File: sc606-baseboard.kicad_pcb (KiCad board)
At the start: 6 copper layers, 100 x 90 mm, 454 parts, among them IC1 TPS54561DPRT, IC2 TPS7A0518PDBVT, IC3 HD3SS3220, IC4 HD3SS3220, J1 PJ-202A, J10 WE_632723300011, J11 USB-A3-C31-D-RA-CS1, J12 U_FL-R-SMT-1_10_, J13 USB-A3-C31-D-RA-CS1, J2 WE_68715014522, J3 F52R-1A7H1-11020, J4 46756-1001, J5 U_FL-R-SMT-1_10_, J6 U_FL-R-SMT-1_10_, J7 DM3AT-SF-PEJM5, J8 693022010811, J9 0473460001, M1 SC606T, Q1 BSS138APW, Q2 BSS138-7-F, Q3 BSS138APW, Q4 BSS138APW, Q5 BSS138APW, Q6 BSS138APW, Q7 BSS138-7-F, Q8 BSS138-7-F, SW1 1X03, U1 AP62301WU-7, U10 NCP163ASN330T1G, U11 EMIF06-MSD02N16, U12 FSUSB30MUX, U13 FT232RQ-REEL, U15 USB57442G, U2 AP62301WU-7, U3 AP62301WU-7, U4 74LVC1G123GN, U5 NTS0102GT, U6 PCA9547BS, U7 LT9611UXC, U8 NTS0102GT, U9 TPD13S523PWR, Y1 ABM8G-24.000MHZ-18-D2Y-T, Y2 ABM8G-25.000MHZ-B4Y-T

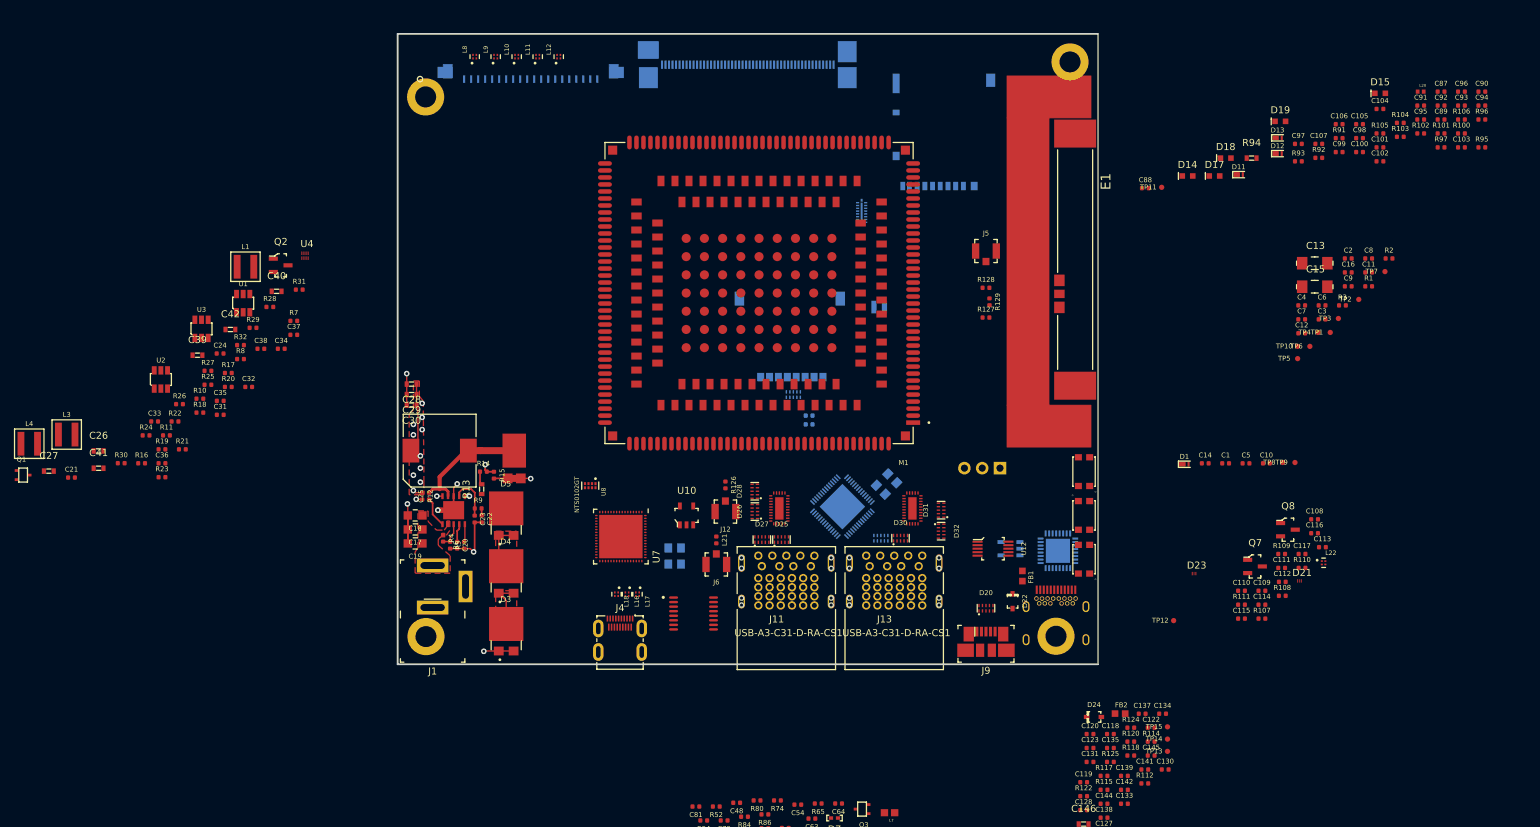
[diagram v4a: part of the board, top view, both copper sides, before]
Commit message: Added buck converters for 3v3 sys, 3v3 cam, 1v2 lontium. Added auto power-on
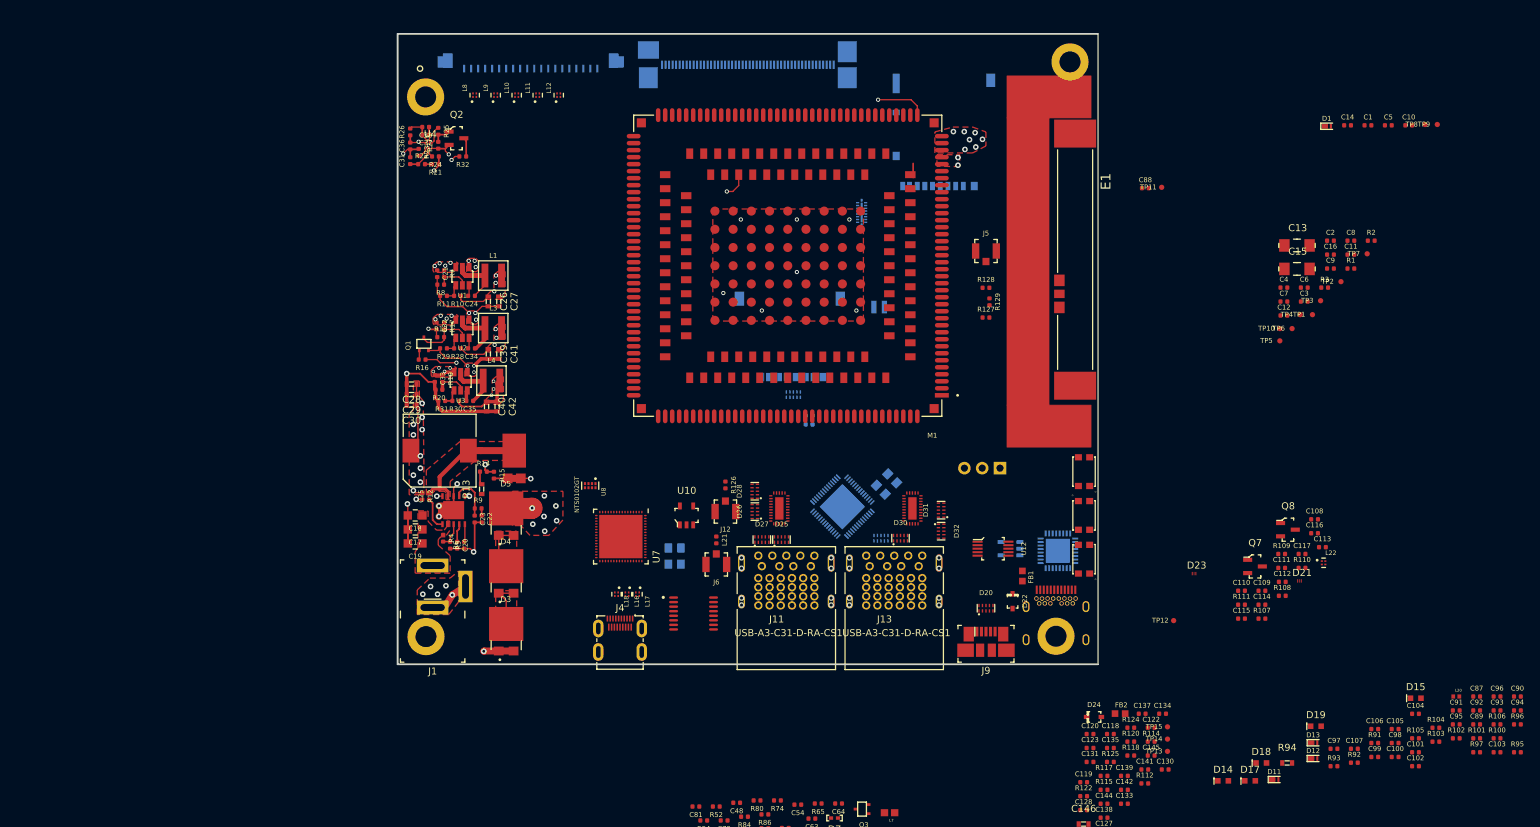
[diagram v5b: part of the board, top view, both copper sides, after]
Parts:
- C146, C158: footprint antmicro-footprints:0603-cap -> sc606-baseboard-footprints:0603-cap
- IC3, IC4: footprint antmicro-footprints:RNH0030A -> sc606-baseboard-footprints:RNH0030A
- J11, J13: footprint antmicro-footprints:USB-A3-C31-D-RA-CS1 -> sc606-baseboard-footprints:USB-A3-C31-D-RA-CS1
- R130, R131, R132, R133, R134, R135, R136, R137, R138, R139, R140, R141, R142, R143, R144, R145, R146, R147, R148, R149, R150, R151, R152, R153, R154, R159, R160, R161: footprint antmicro-footprints:0402-res -> sc606-baseboard-footprints:0402-res
- moved C100 86.5 mm to (217.4, 143.2)
- moved C102 86.5 mm to (220.3, 144.6)
- moved C89 86.5 mm to (229.1, 138.6)
- moved C95 86.5 mm to (226.1, 138.6)
- moved C99 86.5 mm to (214.5, 143.2)
- moved D11 86.5 mm to (200.2, 146.5)
- moved D12 86.5 mm to (205.7, 143.5)
- moved D13 86.5 mm to (205.7, 141.2)
- moved D14 86.5 mm to (192.9, 146.6)
- moved D17 86.5 mm to (196.7, 146.6)
- moved R103 86.5 mm to (223.2, 141.1)
- moved R106 86.5 mm to (232.0, 138.6)
- moved R92 86.5 mm to (211.6, 144.1)
- moved R93 86.5 mm to (208.7, 144.6)
- moved R96 86.5 mm to (234.9, 138.6)
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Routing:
- net V_SOM: track 0.00 -> 81.7 mm, vias 0 -> 14
- net PWRKEY: track 0.00 -> 73.1 mm, vias 0 -> 2
- net GND: track 36.2 -> 94.8 mm, vias 6 -> 33
- net CAM_RST: track 0.00 -> 56.9 mm, vias 0 -> 2
- net 3V3_SYS: track 0.00 -> 9.42 mm, vias 0 -> 3
- net 5V0_SYS: track 15.2 -> 23.8 mm, vias 11 -> 25
- net Net-(Q1-Pad3): track 0.00 -> 8.51 mm
- net Net-(C35-Pad1): track 0.00 -> 7.82 mm
- net Net-(C34-Pad1): track 0.00 -> 7.77 mm
- net Net-(C24-Pad1): track 0.00 -> 7.64 mm
- net 1V2_SYS: track 0.00 -> 4.88 mm, vias 0 -> 3
- net 3V3_CAM: track 0.00 -> 4.64 mm, vias 0 -> 3
- net Net-(R7-Pad2): track 0.00 -> 4.61 mm
- net Net-(R19-Pad2): track 0.00 -> 4.55 mm
- net Net-(C37-Pad2): track 0.00 -> 4.46 mm
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- added copper zone on F.Cu, net 1V2_SYS
- added copper zone on F.Cu, net 3V3_CAM
- added copper zone on F.Cu, net 3V3_SYS
- added copper zone on F.Cu, net GND
- added copper zone on F.Cu, net Net-(C25-Pad2)
- added copper zone on F.Cu, net V_SOM
- added copper zone on In3.5V0, net V_SOM
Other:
- net class Default: clearance 0.2 -> 0.15; trace_width 0.25 -> 0.15; via_dia 0.8 -> 0.6; via_drill 0.4 -> 0.35
- rule trace_clearance: 0.2 -> 0.15
- rule trace_min: 0.2 -> 0.15
- rule via_min_drill: 0.3 -> 0.35
- rule via_min_size: 0.4 -> 0.6

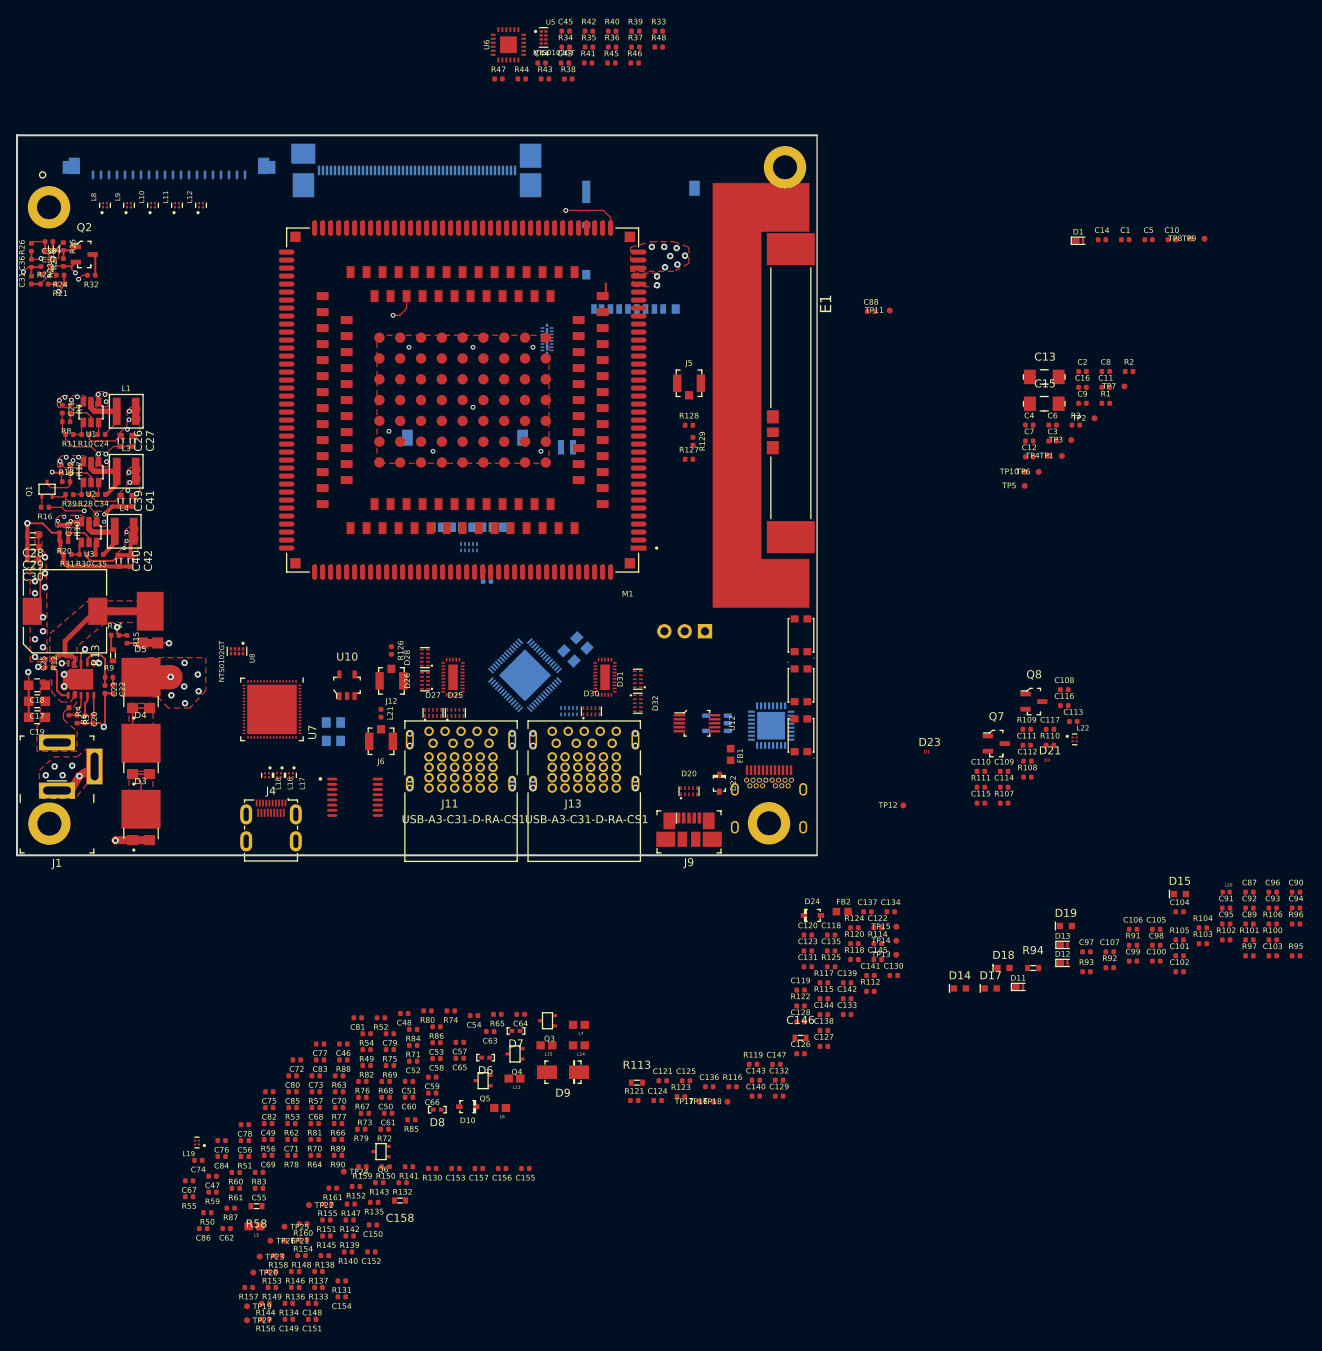
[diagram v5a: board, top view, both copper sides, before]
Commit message: FFC and general display camera connectors distributed on board
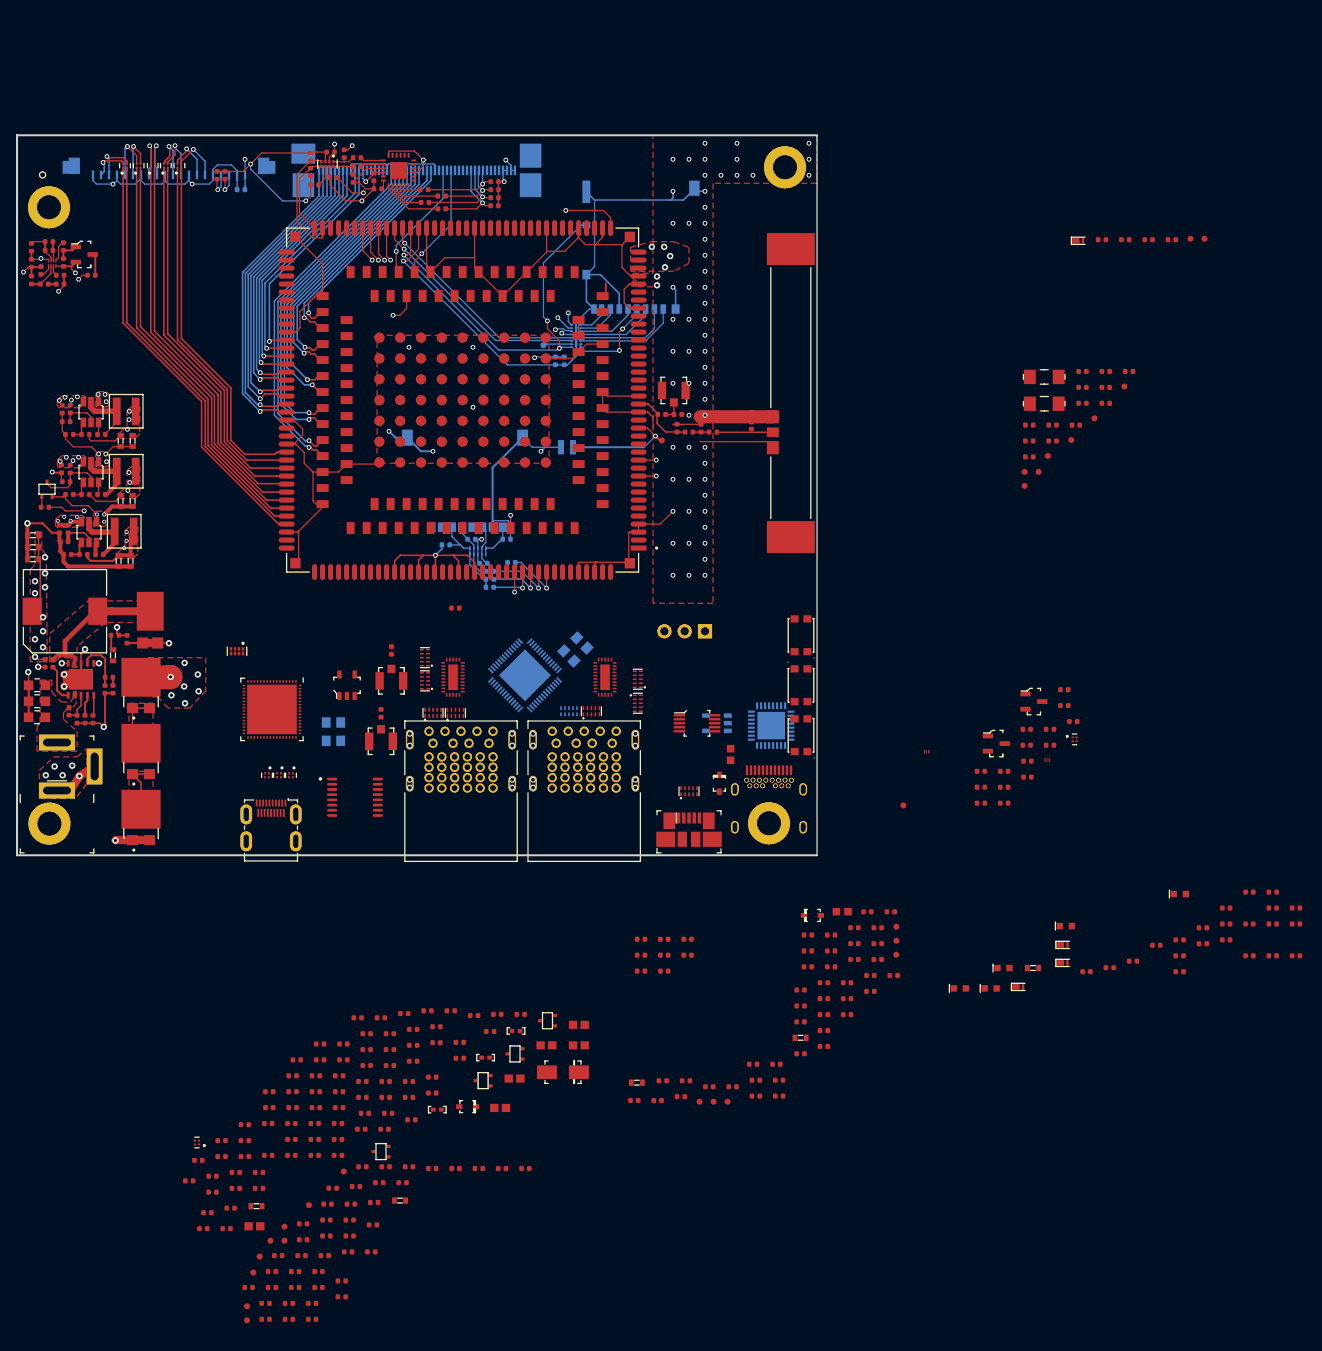
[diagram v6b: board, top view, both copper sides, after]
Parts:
- added C159: C_100n_0402, sc606-baseboard-footprints:0402-cap, F.Cu at (153.0, 140.5)
- added C160: C_100n_0402, sc606-baseboard-footprints:0402-cap, F.Cu at (153.0, 142.5)
- added C161: C_100n_0402, sc606-baseboard-footprints:0402-cap, F.Cu at (155.9, 140.5)
- added C162: C_100n_0402, sc606-baseboard-footprints:0402-cap, F.Cu at (153.0, 144.5)
- added C163: C_100n_0402, sc606-baseboard-footprints:0402-cap, F.Cu at (155.9, 142.5)
- added C164: C_100n_0402, sc606-baseboard-footprints:0402-cap, F.Cu at (158.8, 140.5)
- added C165: C_100n_0402, sc606-baseboard-footprints:0402-cap, F.Cu at (155.9, 144.5)
- added C166: C_100n_0402, sc606-baseboard-footprints:0402-cap, F.Cu at (158.8, 142.5)
- C100, C104, C105, C106, C107, C58, C97, R100, R101, TP11: moved to B.Cu
- moved R55 127.8 mm to (101.0, 45.0), turned to 90 degrees
- moved R56 120.7 mm to (100.0, 45.0), turned to 90 degrees
- moved C58 111.3 mm to (103.0, 46.8)
- moved R100 107.7 mm to (134.1, 95.5), turned to 180 degrees
- moved C100 105.4 mm to (143.4, 68.2), turned to 90 degrees
- moved R101 104.7 mm to (134.1, 96.5), turned to 180 degrees
- moved C104 102.6 mm to (128.6, 91.2), turned to 180 degrees
- moved C97 99.3 mm to (142.3, 68.2), turned to 90 degrees
- moved C90 97.7 mm to (157.6, 74.9)
- moved C105 95.8 mm to (133.3, 93.5), turned to 180 degrees
- moved C107 95.0 mm to (131.8, 90.5)
- moved C106 92.2 mm to (136.2, 90.5)
- moved C92 89.6 mm to (162.0, 77.1), turned to 180 degrees
- moved R91 88.7 mm to (155.6, 74.9)
- moved L20 83.2 mm to (166.8, 76.3), turned to 90 degrees
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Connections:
- net CAM1_DATA_0 renamed CAM1_D0_P
- net CAM1_DATA_1 renamed CAM1_D0_N
- net CAM1_DATA_2 renamed CAM1_D1_P
- net CAM1_DATA_3 renamed CAM1_D1_N
- net CAM1_DATA_4 renamed CAM1_D2_P
- net CAM1_DATA_5 renamed CAM1_D2_N
- net CAM1_DATA_6 renamed CAM1_D3_P
- net CAM1_DATA_7 renamed CAM1_D3_N
- net CAM1_DATA_8 renamed CAM1_CLK_P
- net CAM1_DATA_9 renamed CAM1_CLK_N
- net CAM2_DATA_0 renamed CAM2_D0_P
- net CAM2_DATA_1 renamed CAM2_D0_N
- net CAM2_DATA_2 renamed CAM2_D1_P
- net CAM2_DATA_3 renamed CAM2_D1_N
- net CAM2_DATA_4 renamed CAM2_D2_P
- net CAM2_DATA_5 renamed CAM2_D2_N
- net CAM2_DATA_6 renamed CAM2_D3_P
- net CAM2_DATA_7 renamed CAM2_D3_N
- net CAM2_DATA_8 renamed CAM2_CLK_P
- net CAM2_DATA_9 renamed CAM2_CLK_N
- net Net-(C102-Pad1) renamed /USB_HUB_Connectors/USB_C1_SS_C_TX2_N
- net Net-(C138-Pad1) renamed /USB_HUB_Connectors/USB_C1_SS_C_TX1_P
- net Net-(C141-Pad1) renamed /USB_HUB_Connectors/USB_C1_SS_C_TX1_N
- net Net-(C147-Pad1) renamed /USB_HUB_Connectors/USB_C2_SS_C_TX1_P
- net Net-(C148-Pad1) renamed /USB_HUB_Connectors/USB_C2_SS_C_TX2_P
- net Net-(C149-Pad1) renamed /USB_HUB_Connectors/USB_C2_SS_C_TX1_N
- net Net-(C150-Pad1) renamed /USB_HUB_Connectors/USB_C2_SS_C_TX2_N
- net Net-(C153-Pad1) renamed /USB_HUB_Connectors/USB_C2_SS_C_RX2_N
- net Net-(C154-Pad1) renamed /USB_HUB_Connectors/USB_C2_SS_C_RX1_N
- net Net-(C155-Pad1) renamed /USB_HUB_Connectors/USB_C2_SS_C_RX2_P
- net Net-(C156-Pad1) renamed /USB_HUB_Connectors/USB_C2_SS_C_RX1_P
- net Net-(C71-Pad1) renamed /display module/TX_D2_C_P
- net Net-(C72-Pad1) renamed /display module/TX_D2_C_N
- net Net-(C73-Pad1) renamed /display module/TX_D1_C_P
- net Net-(C74-Pad1) renamed /display module/TX_D1_C_N
- net Net-(C75-Pad1) renamed /display module/TX_D0_C_P
- net Net-(C76-Pad1) renamed /display module/TX_D0_C_N
- net Net-(C77-Pad1) renamed /display module/TX_CLK_C_P
- net Net-(C78-Pad1) renamed /display module/TX_CLK_C_N
- net Net-(C94-Pad1) renamed /USB_HUB_Connectors/USB_C1_SS_C_TX2_P
- net Net-(IC3-Pad10) renamed /USB_HUB_Connectors/USB_C1_SS_C_RX_N
- net Net-(IC3-Pad6) renamed /USB_HUB_Connectors/USB_C1_SS_C_TX_P
- net Net-(IC3-Pad7) renamed /USB_HUB_Connectors/USB_C1_SS_C_TX_N
- net Net-(IC3-Pad9) renamed /USB_HUB_Connectors/USB_C1_SS_C_RX_P
- net Net-(IC4-Pad10) renamed /USB_HUB_Connectors/USB_C2_SS_C_RX_N
- net Net-(IC4-Pad6) renamed /USB_HUB_Connectors/USB_C2_SS_C_TX_P
- net Net-(IC4-Pad7) renamed /USB_HUB_Connectors/USB_C2_SS_C_TX_N
- net Net-(IC4-Pad9) renamed /USB_HUB_Connectors/USB_C2_SS_C_RX_P
- net Net-(J3-Pad11) renamed /display module/SoMtoDisplay_Ferr_D0_N
- net Net-(J3-Pad12) renamed /display module/SoMtoDisplay_Ferr_D0_P
- net Net-(J3-Pad14) renamed /display module/SoMtoDisplay_Ferr_CLK_N
- net Net-(J3-Pad15) renamed /display module/SoMtoDisplay_Ferr_CLK_P
- net Net-(J3-Pad2) renamed /display module/SoMtoDisplay_Ferr_D3_N
- net Net-(J3-Pad3) renamed /display module/SoMtoDisplay_Ferr_D3_P
- net Net-(J3-Pad5) renamed /display module/SoMtoDisplay_Ferr_D2_N
- net Net-(J3-Pad6) renamed /display module/SoMtoDisplay_Ferr_D2_P
- net Net-(J3-Pad8) renamed /display module/SoMtoDisplay_Ferr_D1_N
- net Net-(J3-Pad9) renamed /display module/SoMtoDisplay_Ferr_D1_P
- net Net-(J4-Pad11) renamed /display module/TX_D0_Ferr_N
- net Net-(J4-Pad12) renamed /display module/TX_CLK_Ferr_P
- net Net-(J4-Pad14) renamed /display module/TX_CLK_Ferr_N
- net Net-(J4-Pad3) renamed /display module/TX_D2_Ferr_P
- net Net-(J4-Pad5) renamed /display module/TX_D2_Ferr_N
- net Net-(J4-Pad6) renamed /display module/TX_D1_Ferr_P
- net Net-(J4-Pad8) renamed /display module/TX_D1_Ferr_N
- net Net-(J4-Pad9) renamed /display module/TX_D0_Ferr_P
- net Net-(L22-Pad1) renamed /USB_flash_debug/SoM_USB_Ferr_D_P
- net Net-(L22-Pad4) renamed /USB_flash_debug/SoM_USB_Ferr_D_N
- net SoMtoDisplay_DATA_0 renamed SoMtoDisplay_D0_P
- net SoMtoDisplay_DATA_1 renamed SoMtoDisplay_D0_N
- net SoMtoDisplay_DATA_2 renamed SoMtoDisplay_D1_P
- net SoMtoDisplay_DATA_3 renamed SoMtoDisplay_D1_N
- net SoMtoDisplay_DATA_4 renamed SoMtoDisplay_D2_P
- net SoMtoDisplay_DATA_5 renamed SoMtoDisplay_D2_N
- net SoMtoDisplay_DATA_6 renamed SoMtoDisplay_D3_P
- net SoMtoDisplay_DATA_7 renamed SoMtoDisplay_D3_N
- net SoMtoDisplay_DATA_8 renamed SoMtoDisplay_CLK_P
- net SoMtoDisplay_DATA_9 renamed SoMtoDisplay_CLK_N
- net SoMtoHDMI_DATA_0 renamed SoMtoLT_D0_P
- net SoMtoHDMI_DATA_1 renamed SoMtoLT_D0_N
- net SoMtoHDMI_DATA_2 renamed SoMtoLT_D1_P
- net SoMtoHDMI_DATA_3 renamed SoMtoLT_D1_N
- net SoMtoHDMI_DATA_4 renamed SoMtoLT_D2_P
- net SoMtoHDMI_DATA_5 renamed SoMtoLT_D2_N
- net SoMtoHDMI_DATA_6 renamed SoMtoLT_D3_P
- net SoMtoHDMI_DATA_7 renamed SoMtoLT_D3_N
- net SoMtoHDMI_DATA_8 renamed SoMtoLT_CLK_P
- net SoMtoHDMI_DATA_9 renamed SoMtoLT_CLK_N
- C92 pad 2: ANT_MAIN -> Net-(C92-Pad2)
- E1 pad 1: Net-(E1-Pad1) -> Net-(C92-Pad1)
- J11 pad 5: /USB_HUB_Connectors/USB_A1_SS_RX_N -> /USB_HUB_Connectors/USB_A1_SS_C_RX_N
- J11 pad 6: /USB_HUB_Connectors/USB_A1_SS_RX_P -> /USB_HUB_Connectors/USB_A1_SS_C_RX_P
- J11 pad 8: /USB_HUB_Connectors/USB_A1_SS_TX_N -> /USB_HUB_Connectors/USB_A1_SS_C_TX_N
- J11 pad 9: /USB_HUB_Connectors/USB_A1_SS_TX_P -> /USB_HUB_Connectors/USB_A1_SS_C_TX_P
- J13 pad 5: /USB_HUB_Connectors/USB_A2_SS_RX_N -> /USB_HUB_Connectors/USB_A2_SS_C_RX_N
- J13 pad 6: /USB_HUB_Connectors/USB_A2_SS_RX_P -> /USB_HUB_Connectors/USB_A2_SS_C_RX_P
- J13 pad 8: /USB_HUB_Connectors/USB_A2_SS_TX_N -> /USB_HUB_Connectors/USB_A2_SS_C_TX_N
- J13 pad 9: /USB_HUB_Connectors/USB_A2_SS_TX_P -> /USB_HUB_Connectors/USB_A2_SS_C_TX_P
- R128 pad 1: Net-(C92-Pad1) -> ANT_MAIN
- R128 pad 2: Net-(E1-Pad1) -> Net-(C92-Pad2)
- R129 pad 1: Net-(E1-Pad1) -> Net-(C92-Pad2)
- U11 pad 18: (no net) -> GND
- U11 pad 19: (no net) -> GND
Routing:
- net GND: track 94.8 -> 443.5 mm, vias 33 -> 99
- net LDO6_1P8: track 0.00 -> 120.6 mm, vias 0 -> 3
- net 3V3_SYS: track 9.42 -> 120.8 mm, vias 3 -> 5
- net LDO17_2P85: track 0.00 -> 95.4 mm, vias 0 -> 2
- net 3V3_CAM: track 4.64 -> 82.8 mm, vias 3 -> 4
- net TP0_I2C_SCL: track 0.00 -> 71.5 mm, vias 0 -> 2
- net 5V0_SYS: track 23.8 -> 89.1 mm, vias 25 -> 26
- net TP0_I2C_SDA: track 0.00 -> 60.5 mm, vias 0 -> 2
- net SoMtoDisplay_D3_N: track 0.00 -> 53.6 mm
- net SoMtoDisplay_D3_P: track 0.00 -> 52.7 mm
- net SoMtoDisplay_D2_N: track 0.00 -> 51.5 mm
- net SoMtoDisplay_D2_P: track 0.00 -> 50.6 mm
- net SoMtoDisplay_D1_N: track 0.00 -> 49.3 mm
- net SD_DATA_6: track 0.00 -> 49.0 mm, vias 0 -> 3
- net SoMtoDisplay_D1_P: track 0.00 -> 48.4 mm
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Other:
- net class CSI_DSI_Inner added: clearance 0.15, trace_width 0.15, via_dia 0.6, via_drill 0.35
- net class CSI_DSI_Outer added: clearance 0.15, trace_width 0.15, via_dia 0.6, via_drill 0.35
- net class HDMI_Inner added: clearance 0.15, trace_width 0.15, via_dia 0.6, via_drill 0.35
